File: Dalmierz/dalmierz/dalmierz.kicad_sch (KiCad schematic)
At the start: 59 parts, among them IC1 W25Q16JVUXIQ, J1 690-005-298-486, J4 4328 URM13, J5 4328 LCD I2C, J6 4328 TF LUNA, Q1 DMG1012T, SW1 SW_Push, SW2 SW_Push, SW3 SW_Push, SW4 SW_Push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

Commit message: MAIN: poprawilem wersje 1 sch.
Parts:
- removed C3: 1n, symbol Device:C
- removed D2: Green, symbol Device:LED
- removed J2: ~, symbol CON_PICO_40W:CON_PICO_40W
- removed J3: ~, symbol CON_PICO_3W:CON_PICO_3W
- removed J4: 4328 URM13, 4328:ADAFRUIT_4328, symbol 4328:4328
- removed J5: 4328 LCD I2C, 4328:ADAFRUIT_4328, symbol 4328:4328
- removed J6: 4328 TF LUNA, 4328:ADAFRUIT_4328, symbol 4328:4328
- removed Q1: DMG1012T, Package_TO_SOT_SMD:SOT-523, symbol Transistor_FET:DMG1012T
- removed R3: 470R, symbol Device:R
- removed R5: 200k, symbol Device:R
- removed R6: 100k, symbol Device:R
- removed SW1: ~, symbol TP-1221U-K9K5325:TP-1221U-K9K5325
- added J2: B4B-ZR_LF__SN_TF LUNA, B4B-ZR_LF__SN_:JST_B4B-ZR_LF__SN_, symbol B4B-ZR_LF__SN_:B4B-ZR_LF__SN_
- added J3: B4B-ZR_LF__SN_LCD I2C, B4B-ZR_LF__SN_:JST_B4B-ZR_LF__SN_, symbol B4B-ZR_LF__SN_:B4B-ZR_LF__SN_
- added J7: B4B-ZR_LF__SN_URM13, B4B-ZR_LF__SN_:JST_B4B-ZR_LF__SN_, symbol B4B-ZR_LF__SN_:B4B-ZR_LF__SN_
- added SW7: SW_Push, symbol Switch:SW_Push
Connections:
- net +3V3: now also J3.2 (VCC), J7.2 (VCC)
- net +5V: now also J2.2 (VCC)
- net GND: now also J2.1 (GND), J3.1 (GND), J7.1 (GND), SW7.1
- net SCL0: now also J2.4 (SCL), J3.4 (SCL), J7.4 (SCL)
- net SDA0: now also J2.3 (SDA), J3.3 (SDA), J7.3 (SDA)
- net at R1.1: now also SW7.2
- net GPIO11: no longer names the net of U1.14 (GPIO11)
- net GPIO14: no longer names the net of U1.17 (GPIO14)
- net GPIO15: no longer names the net of U1.18 (GPIO15)
- net GPIO16: no longer names the net of U1.27 (GPIO16)
- net GPIO17: no longer names the net of U1.28 (GPIO17)
- net GPIO18: no longer names the net of U1.29 (GPIO18)
- net GPIO19: no longer names the net of U1.30 (GPIO19)
- net GPIO20: no longer names the net of U1.31 (GPIO20)
- net GPIO21: no longer names the net of U1.32 (GPIO21)
- net GPIO22: no longer names the net of U1.34 (GPIO22)
- net GPIO23: no longer names the net of U1.35 (GPIO23)
- net GPIO24: no longer names the net of U1.36 (GPIO24)
- net GPIO25: no longer names the net of U1.37 (GPIO25)
- net GPIO26_ADC0: no longer names the net of U1.38 (GPIO26_ADC0)
- net GPIO27_ADC1: no longer names the net of U1.39 (GPIO27_ADC1)
- net GPIO28_ADC2: no longer names the net of U1.40 (GPIO28_ADC2)
- net GPIO29_ADC3: no longer names the net of U1.41 (GPIO29_ADC3)
- net SWCLK: no longer names the net of U1.24 (SWCLK)
- net SWDIO: no longer names the net of U1.25 (SWD)
- no-connect marks 15 -> 34
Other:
- note removed: "ADC GPIO"
- note removed: "CON PICO"
- note removed: "DEBUG"
- note removed: "LED"
- moved on the sheet: C16, C17, J1, R14, SW1, SW2, SW3, SW4, SW5, SW6, Y1

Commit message: MAIN: footprinty work in progress.
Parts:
- removed SW1, SW2, SW3, SW4, SW5, SW6, SW7: SW_Push, symbol Switch:SW_Push
- added SW1, SW2, SW3, SW4, SW5, SW6, SW7: 1-1825910-4, 1-1825910-4:TE_1-1825910-4, symbol 1-1825910-4:1-1825910-4
- C1, C2: footprint (none) -> Capacitor_SMD:C_0805_2012Metric
- C10, C11, C15, C4, C5, C6, C7, C8, C9: footprint (none) -> Capacitor_SMD:C_0603_1608Metric
- C12, C13, C14, C18: value 2u2 -> 2.2u; footprint (none) -> Capacitor_SMD:C_0805_2012Metric
- C16, C17: footprint (none) -> kondensatory:15p-CAPC1005X55N
- C19, C20: footprint (none) -> kondensatory:1u-CAPC4532X229N
- C21, C22: value 2.2uF -> 2.2u; footprint (none) -> Capacitor_SMD:C_0805_2012Metric
- L1: value 2u2 -> 2.2u; footprint (none) -> Inductor_SMD:L_0603_1608Metric
- R1, R12, R13, R14, R4, R8: footprint (none) -> Resistor_SMD:R_1210_3225Metric
- R7: footprint (none) -> Resistor_SMD:R_0805_2012Metric
- R9: footprint (none) -> Resistor_SMD:R_1206_3216Metric
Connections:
- net BTN1: now also SW1.1
- net BTN2: now also SW2.1
- net BTN3: now also SW3.1
- net BTN4: now also SW4.1
- net BTN5: now also SW5.1
- net BTN6: now also SW6.1
- net GND: now also SW1.4, SW2.4, SW3.4, SW4.4, SW5.4, SW6.4, SW7.1
- net at R1.1: now also SW7.4
- no-connect marks 34 -> 48

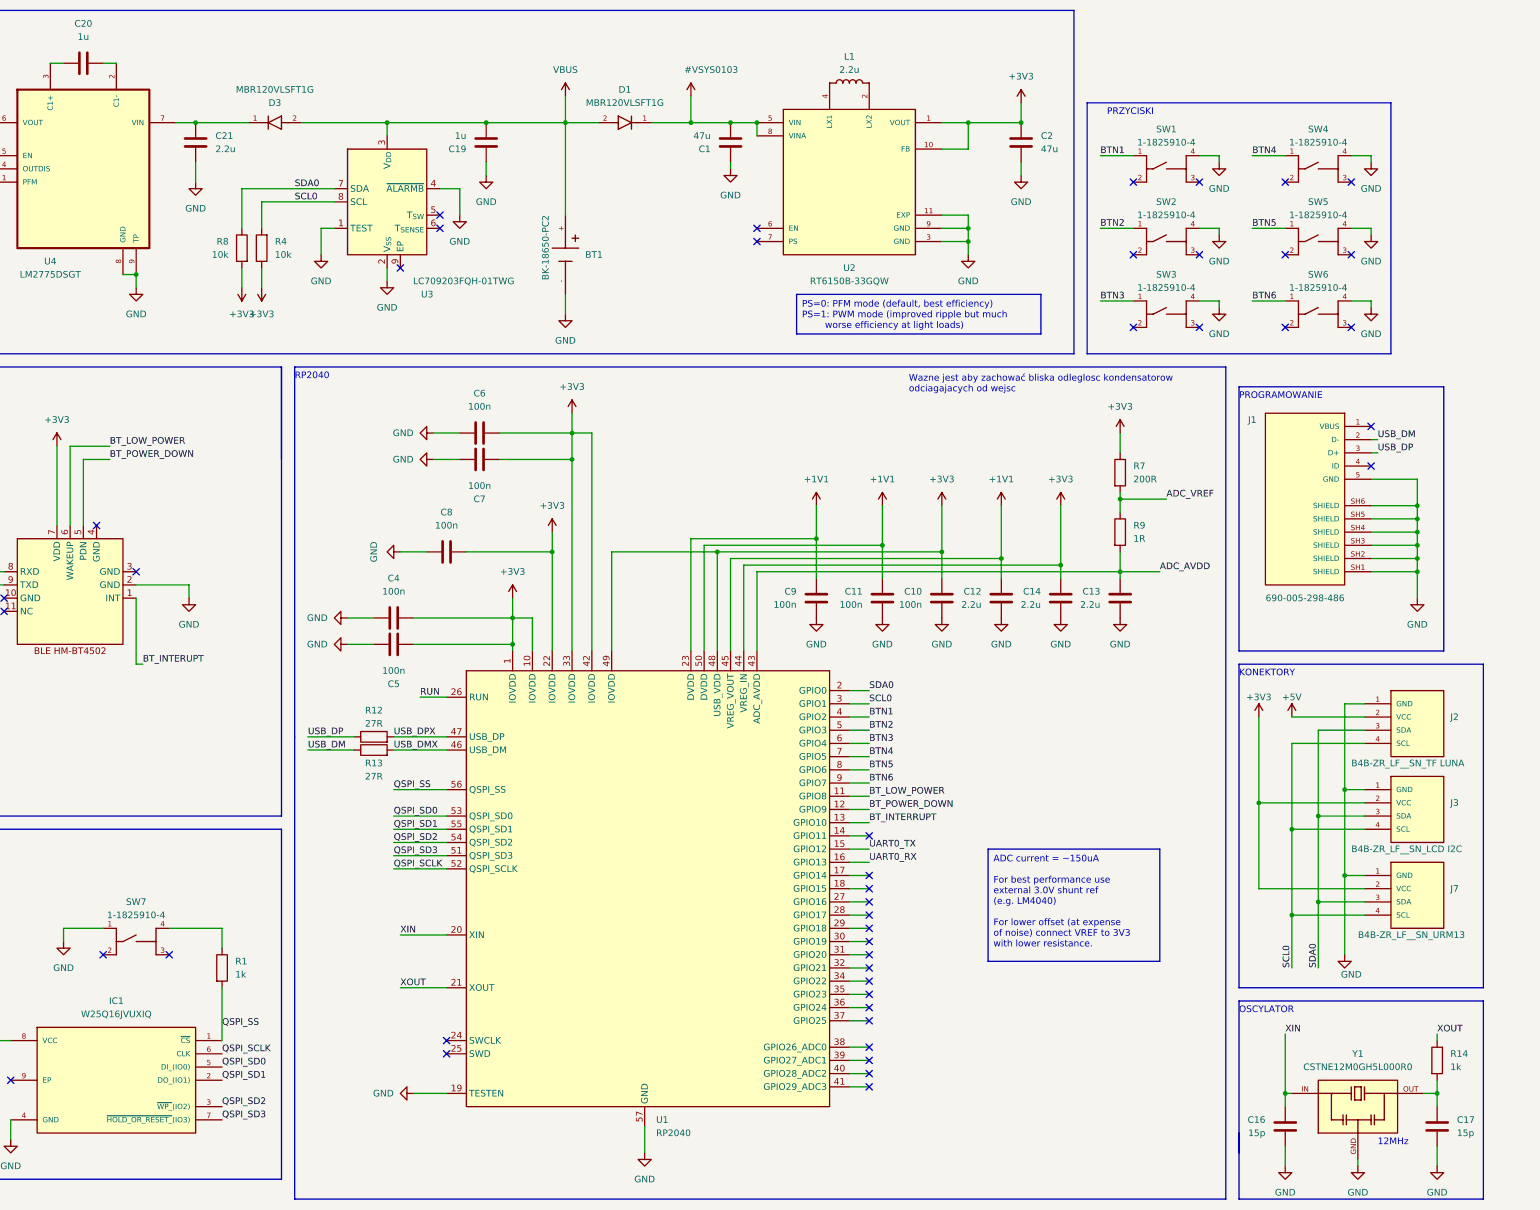
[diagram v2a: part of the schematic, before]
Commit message: MAIN: PCB, rozmieszczenie komponentow.
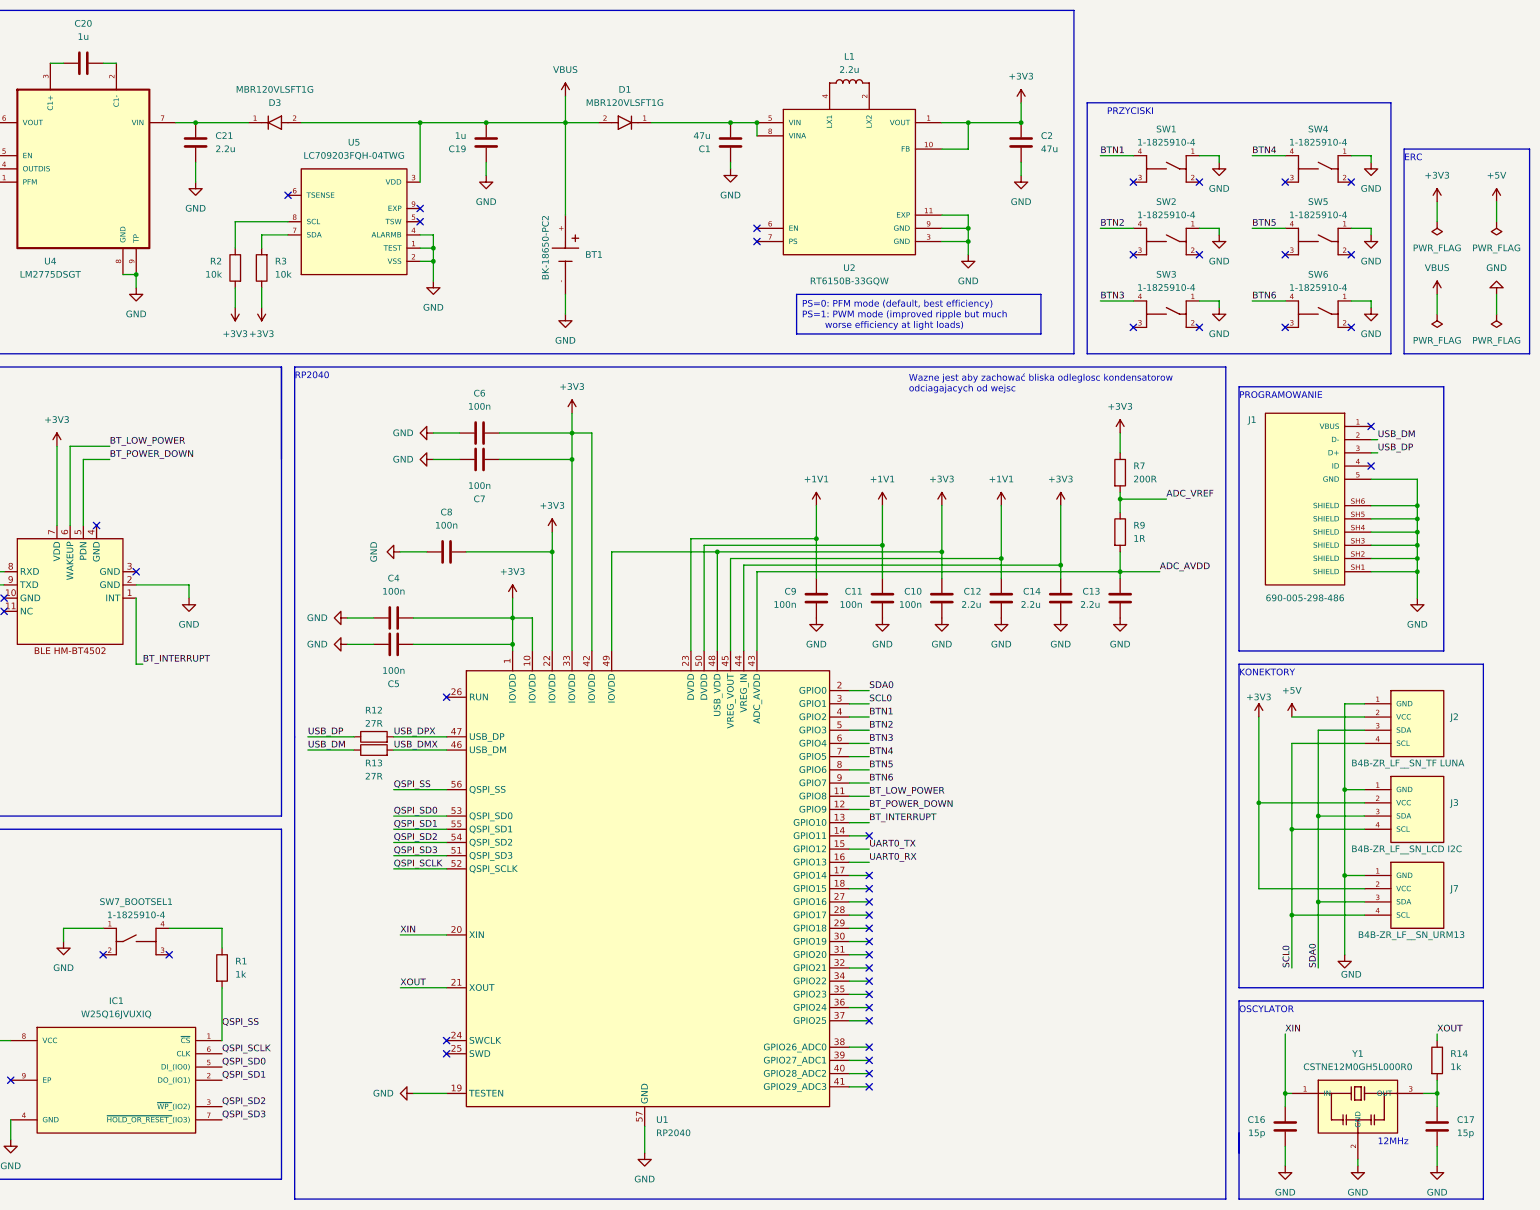
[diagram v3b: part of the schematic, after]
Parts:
- removed R4, R8: 10k, Resistor_SMD:R_1210_3225Metric, symbol Device:R
- removed U3: LC709203FQH-01TWG, Package_DFN_QFN:WDFN-8-1EP_4x3mm_P0.65mm_EP2.4x1.8mm, symbol Battery_Management:LC709203FQH-01TWG
- added R2, R3: 10k, Resistor_SMD:R_1210_3225Metric, symbol Device:R
- added U5: LC709203FQH-04TWG, LC709203FQH-04TWG:DFN300X400X80-8N, symbol LC709203FQH-04TWG:LC709203FQH-04TWG
- B1: footprint (none) -> BLE_HM-BT4502:BLE_HM-BT5402
- C16, C17: footprint kondensatory:15p-CAPC1005X55N -> Capacitor_SMD:C_1210_3225Metric
- C19, C20: footprint kondensatory:1u-CAPC4532X229N -> Capacitor_SMD:C_1206_3216Metric
- renumbered SW7 to SW7_BOOTSEL1
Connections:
- net BT_INTERUPT is gone; now on net BT_INTERRUPT: B1.1 (INT)
- net +3V3: now also R2.2, R3.1
- net BTN1: now also SW1.4; no longer SW1.1
- net BTN2: now also SW2.4; no longer SW2.1
- net BTN3: now also SW3.4; no longer SW3.1
- net BTN4: now also SW4.4; no longer SW4.1
- net BTN5: now also SW5.4; no longer SW5.1
- net BTN6: now also SW6.4; no longer SW6.1
- net GND: now also SW1.1, SW2.1, SW3.1, SW4.1, SW5.1, SW6.1, Y1.2 (GND), U5.1 (TEST), U5.2 (VSS), U5.4 (ALARMB); no longer SW1.4, SW2.4, SW3.4, SW4.4, SW5.4, SW6.4, Y1.GND
- net VBUS: now also U5.3 (VDD)
- net XIN: now also Y1.1 (IN); no longer Y1.IN
- net at C17.1, R14.2: now also Y1.3 (OUT); no longer Y1.OUT
- net RUN: no longer names the net of U1.26 (RUN)
- new net: R3.2, U5.7 (SDA)
- new net: R2.1, U5.8 (SCL)
- no-connect marks 48 -> 49
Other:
- note added: "ERC"
- company: (none) -> Politechnika Poznańska
- title: (none) -> Projekt PUEIE - Dalmierz

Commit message: MAIN: footprinty, rozmieszczenie na PCB work in progress
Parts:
- C1, C12, C13, C14, C18, C2, C21, C22: footprint Capacitor_SMD:C_0805_2012Metric -> Capacitor_SMD:C_0603_1608Metric
- C16, C17: footprint Capacitor_SMD:C_1210_3225Metric -> Capacitor_SMD:C_0603_1608Metric
- C19, C20: footprint Capacitor_SMD:C_1206_3216Metric -> Capacitor_SMD:C_0603_1608Metric
- R11: renamed from R1; footprint Resistor_SMD:R_1210_3225Metric -> Resistor_SMD:R_0603_1608Metric
- R12, R13, R14, R2, R3: footprint Resistor_SMD:R_1210_3225Metric -> Resistor_SMD:R_0603_1608Metric
- R7: footprint Resistor_SMD:R_0805_2012Metric -> Resistor_SMD:R_0603_1608Metric
- R9: footprint Resistor_SMD:R_1206_3216Metric -> Resistor_SMD:R_0603_1608Metric
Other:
- note added: "ADC_VREF zostawiamy rozłączone. Mimo, że nie wykorzystujemy ADC w naszym projekcie to ADC_AVDD pozostaje zasilane ze wzgledu na wewnętrzne połączenia w RP2040."
- note added: "Ponieważ wykorzystujemy USB_DB i USB_DM konieczne jest zasilenie USB_VDD. W przypadku nie wykorzystanie USB w projekcie i tak powinniśmy zostawić USB_VDD podłączne do zasilania."
- note added: "Ważne jest aby zachować bliską odległość kondensatorów odciągających od wejść."
- note removed: "Wazne jest aby zachować bliska odleglosc kondensatorow odciagajacych od wejsc"
- moved on the sheet: C15, C18

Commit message: MAIN: PCB traces in progress.
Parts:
- renumbered SW7_BOOTSEL1 to SW7
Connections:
- net SCL0: now also R2.1, U5.8 (SCL)
- net SDA0: now also R3.2, U5.7 (SDA)
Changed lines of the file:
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@@
+    (effects (font (size 1.27 1.27)) (justify left bottom))
+  )
+  (label "SDA0" (at 86.36 58.42 0) (fields_autoplaced)
     (effects (font (size 1.27 1.27)) (justify left bottom))
   )
@@
   )
   (label "QSPI_SD0" (at 111.76 170.18 0) (fields_autoplaced)
+    (effects (font (size 1.27 1.27)) (justify left bottom))
+  )
+  (label "SCL0" (at 81.28 55.88 0) (fields_autoplaced)
     (effects (font (size 1.27 1.27)) (justify left bottom))
   )
@@
   (symbol (lib_id "1-1825910-4:1-1825910-4") (at 60.96 194.31 0) (unit 1)
     (in_bom yes) (on_board yes) (dnp no) (fields_autoplaced)
-    (property "Reference" "SW7_BOOTSEL1" (at 62.23 186.69 0)
+    (property "Reference" "SW7" (at 62.23 186.69 0)
       (effects (font (size 1.27 1.27)))
     )
@@
       (project "dalmierz"
         (path "/785c36ae-1f77-43ce-9999-38f24abdc22e"
-          (reference "SW7_BOOTSEL1") (unit 1)
+          (reference "SW7") (unit 1)
         )
       )
@@
   )
   (symbol (lib_id "RP2040_CUSTOM:RP2040") (at 160.02 184.15 0) (unit 1)
-    (in_bom yes) (on_board yes) (dnp no) (fields_autoplaced)
+    (in_bom yes) (on_board yes) (dnp no)
     (property "Reference" "U1" (at 162.2141 228.6 0)
       (effects (font (size 1.27 1.27)) (justify left))
